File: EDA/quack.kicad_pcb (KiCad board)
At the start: 2 copper layers, 56.6 x 57.7 mm, 25 parts, among them IC1 ESP32-PICO-D4, IC2 TXB0108PWR, J1 DIN-4, J2 DB9_Male, J3 FTDI, J4 MODE, U1 AMS1117-3.3

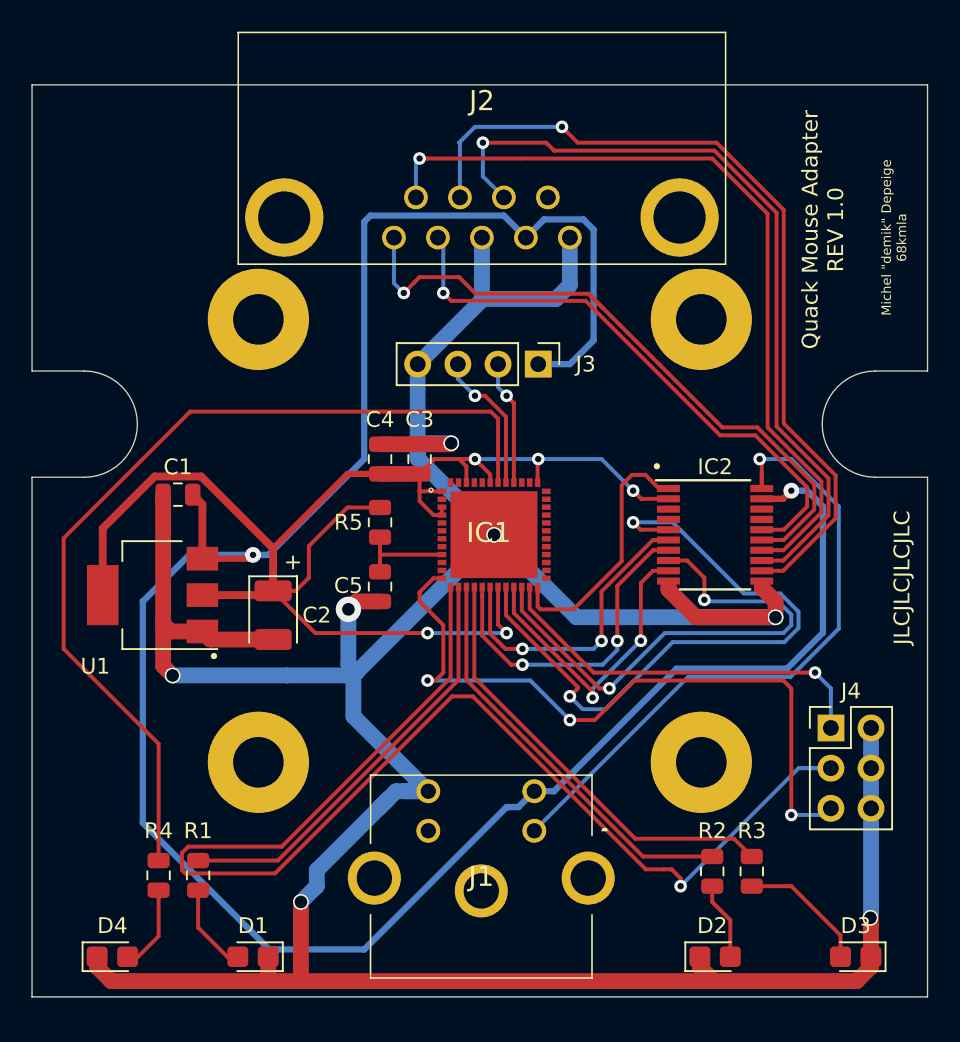
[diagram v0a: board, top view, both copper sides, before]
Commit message: added pin usage text + logos
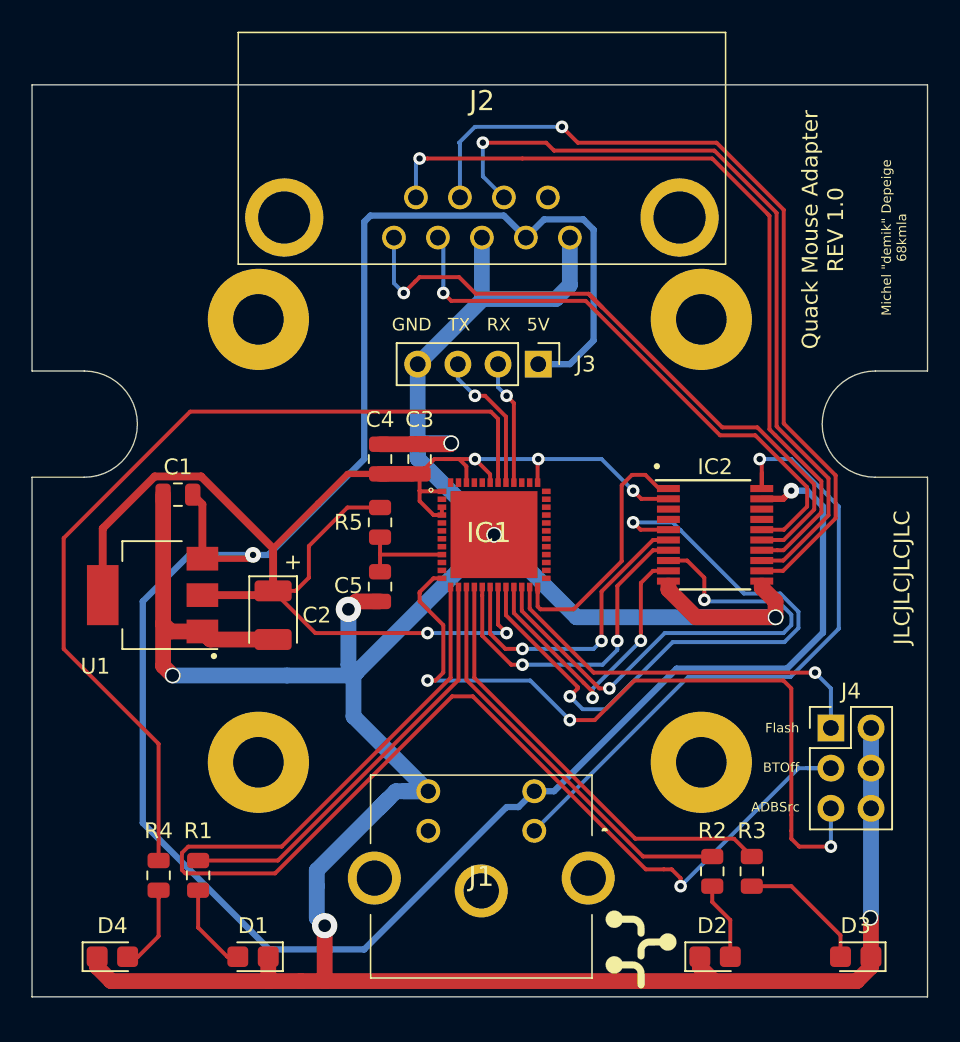
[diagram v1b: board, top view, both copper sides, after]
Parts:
- added G***: LOGO, ADB_logo_5mm:ADB_logo_5mm, F.Cu at (165.5, 124.0)
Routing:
- net ADBSRC: track 44.6 -> 49.2 mm
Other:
- board text added: "5V"
- board text added: "ADBSrc"
- board text added: "BTOff"
- board text added: "Flash"
- board text added: "GND"
- board text added: "RX"
- board text added: "TX"

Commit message: added beads to reduce EMI
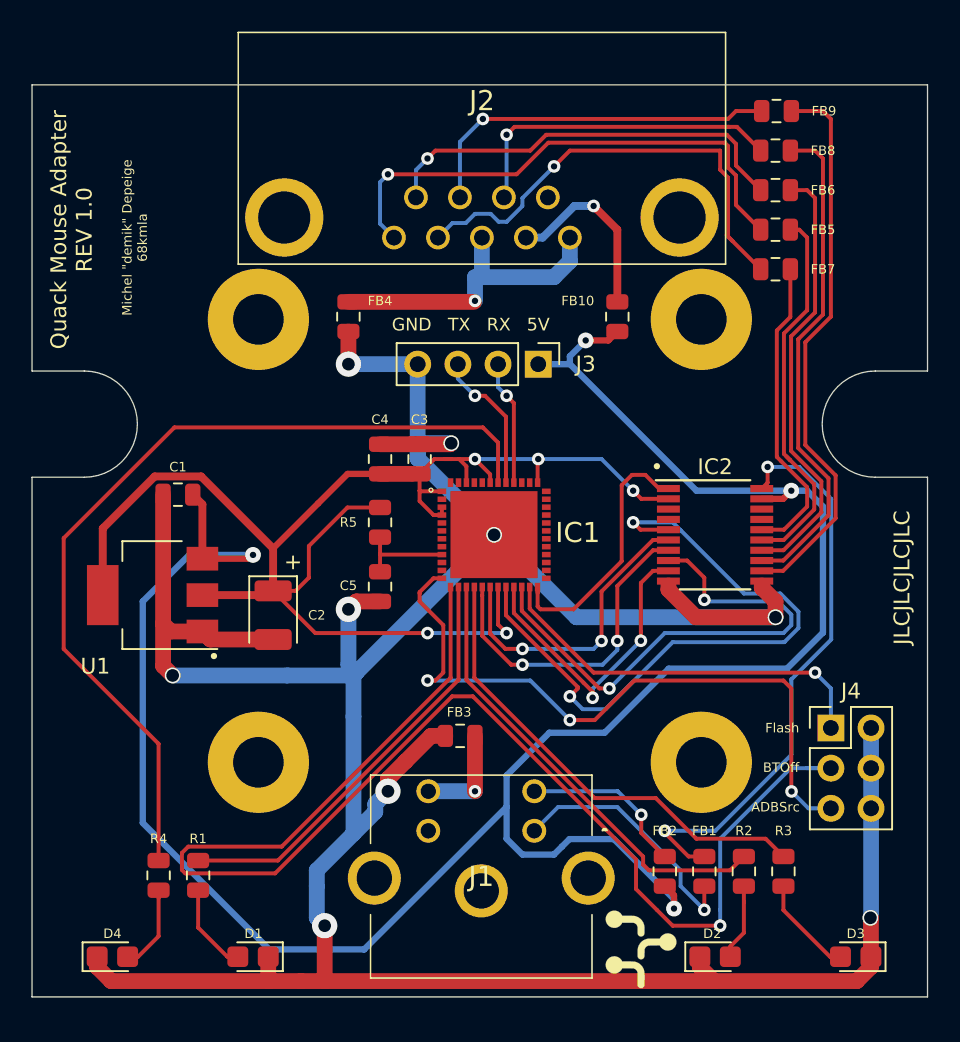
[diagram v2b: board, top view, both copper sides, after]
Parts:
- added FB1: Ferrite_Bead, Inductor_SMD:L_0805_2012Metric, F.Cu at (169.5, 119.1)
- added FB10: Ferrite_Bead_Small, Inductor_SMD:L_0805_2012Metric, F.Cu at (164.0, 84.0)
- added FB2: Ferrite_Bead, Inductor_SMD:L_0805_2012Metric, F.Cu at (167.0, 119.1)
- added FB3: Ferrite_Bead, Inductor_SMD:L_0805_2012Metric, F.Cu at (154.1, 110.5)
- added FB4: Ferrite_Bead_Small, Inductor_SMD:L_0805_2012Metric, F.Cu at (147.0, 84.0)
- added FB5: Ferrite_Bead_Small, Inductor_SMD:L_0805_2012Metric, F.Cu at (174.0, 78.5)
- added FB6: Ferrite_Bead_Small, Inductor_SMD:L_0805_2012Metric, F.Cu at (174.0, 76.0)
- added FB7: Ferrite_Bead_Small, Inductor_SMD:L_0805_2012Metric, F.Cu at (174.0, 81.0)
- added FB8: Ferrite_Bead_Small, Inductor_SMD:L_0805_2012Metric, F.Cu at (174.0, 73.5)
- added FB9: Ferrite_Bead_Small, Inductor_SMD:L_0805_2012Metric, F.Cu at (174.1, 71.0)
- moved R2 2.00 mm to (172.0, 119.1)
- moved R3 2.00 mm to (174.5, 119.1)
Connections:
- IC2 pad 20: Net-(IC2-Pad20) -> Net-(FB1-Pad2)
- J1 pad 1: Net-(IC2-Pad20) -> Net-(FB1-Pad1)
- J1 pad 3: +5V -> Net-(FB2-Pad2)
- J1 pad 4: GND -> Net-(FB3-Pad2)
- J2 pad 1: GND -> Net-(FB4-Pad2)
- J2 pad 2: +5V -> Net-(FB10-Pad1)
- J2 pad 3: GND -> Net-(FB4-Pad2)
- J2 pad 4: /quack_connectors/QX2_5V -> Net-(FB7-Pad1)
- J2 pad 5: /quack_connectors/QX1_5V -> Net-(FB5-Pad1)
- J2 pad 7: /quack_connectors/CLICK_5V -> Net-(FB8-Pad1)
- J2 pad 8: /quack_connectors/QY2_5V -> Net-(FB9-Pad1)
- J2 pad 9: /quack_connectors/QY1_5V -> Net-(FB6-Pad1)
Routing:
- net Net-(IC2-Pad20): track 41.4 -> 0.00 mm, vias 1 -> 0
- net Net-(FB1-Pad2): track 0.00 -> 36.8 mm, vias 0 -> 2
- net Net-(FB5-Pad1): track 0.00 -> 33.1 mm, vias 0 -> 1
- net Net-(FB7-Pad1): track 0.00 -> 29.9 mm, vias 0 -> 1
- net Net-(FB6-Pad1): track 0.00 -> 26.7 mm, vias 0 -> 1
- net Net-(FB9-Pad1): track 0.00 -> 23.4 mm, vias 0 -> 1
- net /quack_connectors/QY1_5V: track 51.0 -> 27.8 mm, vias 1 -> 0
- net Net-(FB8-Pad1): track 0.00 -> 21.0 mm, vias 0 -> 1
- net Net-(FB4-Pad2): track 0.00 -> 20.7 mm, vias 0 -> 1
- net /quack_connectors/CLICK_5V: track 50.3 -> 31.7 mm, vias 1 -> 0
- net /quack_connectors/QX1_5V: track 42.5 -> 24.3 mm, vias 1 -> 0
- net /quack_connectors/QY2_5V: track 53.5 -> 35.5 mm, vias 1 -> 0
- net /quack_connectors/QX2_5V: track 36.4 -> 19.6 mm, vias 1 -> 0
- net Net-(FB1-Pad1): track 0.00 -> 16.1 mm, vias 0 -> 1
- net Net-(FB10-Pad1): track 0.00 -> 11.8 mm, vias 0 -> 1
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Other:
- net class +V: via_dia 1 -> 0.8

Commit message: board revision 1.1
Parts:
- added ANT1: Antenna_Shield, RF_Antenna:Texas_SWRA117D_2.4GHz_Right, F.Cu at (134.0, 83.0)
- R1: value 33 -> 39
- R2, R3, R4: value 120 -> 150
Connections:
- IC1 pad 2: (no net) -> Net-(ANT1-Pad1)
- IC1 pad 39: (no net) -> OE
- IC2 pad 10: GND -> OE
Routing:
- net Net-(ANT1-Pad1): track 0.00 -> 24.1 mm
- net OE: track 0.00 -> 20.5 mm, vias 0 -> 2
- net GND: track 205.9 -> 196.0 mm
- net CLICK_3V: track 32.9 -> 26.1 mm
- net QX2_3V: track 42.2 -> 36.1 mm
- net +3V3: track 94.1 -> 98.1 mm, vias 5 -> 7
- net Net-(IC1-Pad42): vias 0 -> 2
- added copper zone on B.Cu, net GND
- added copper zone on F.Cu, net GND
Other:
- board text added: "Quack Mouse Adapter REV 1.1"
- board text removed: "Quack Mouse Adapter REV 1.0"

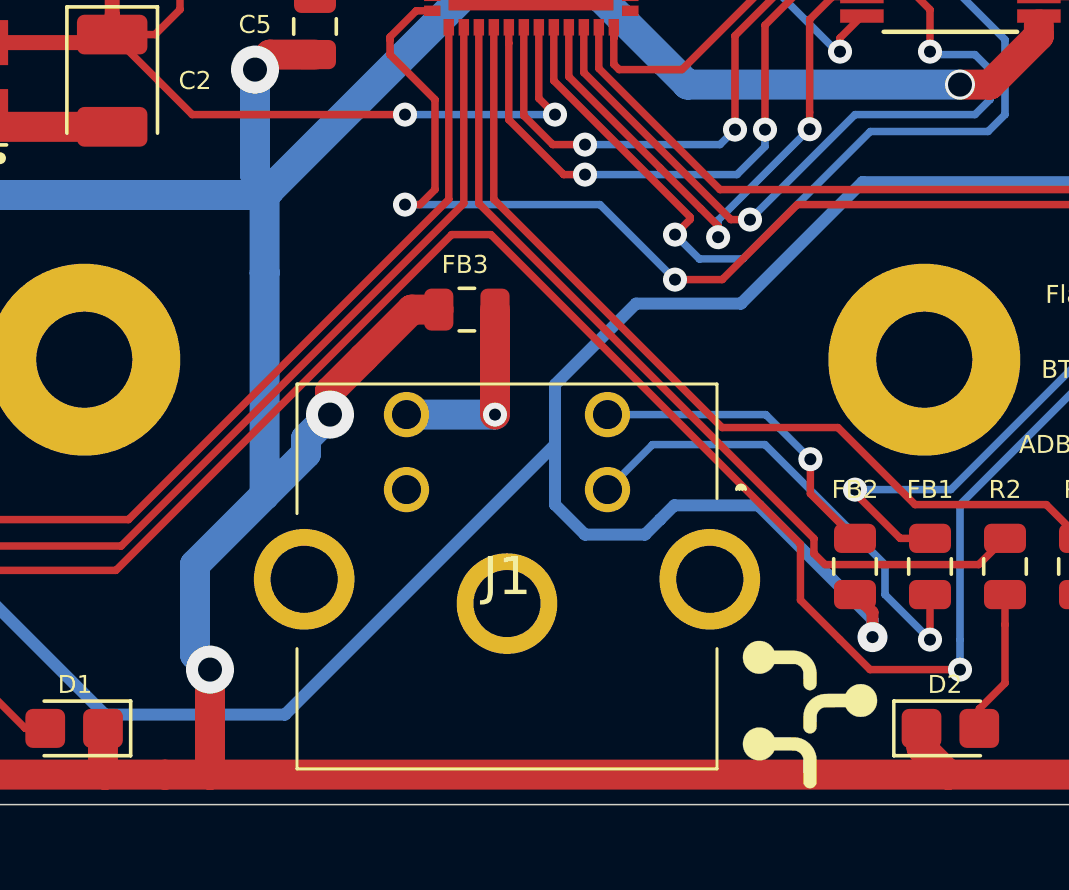
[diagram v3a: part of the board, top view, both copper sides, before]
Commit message: revision 1.2: move ADB socket 2mm out
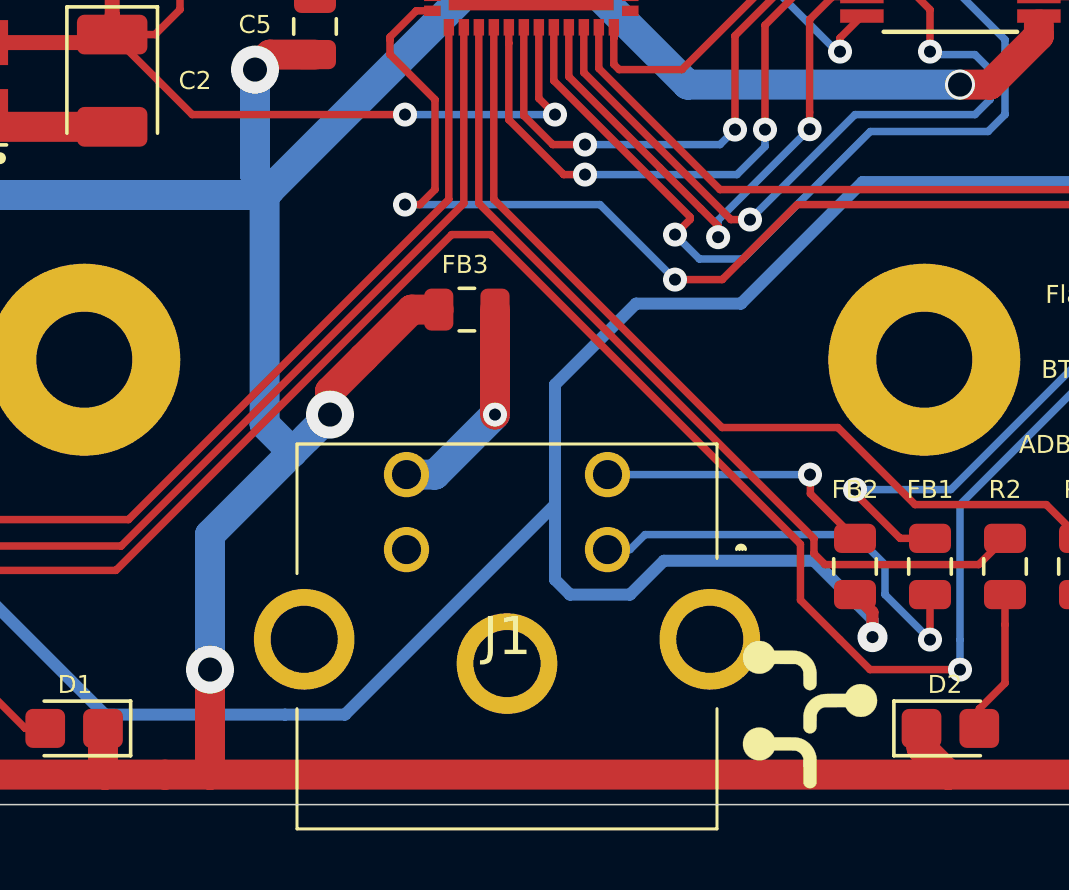
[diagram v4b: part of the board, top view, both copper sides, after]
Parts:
- moved J1 2.00 mm to (158.8, 118.5)
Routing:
- net Net-(FB1-Pad1): track 16.1 -> 14.5 mm
- net Net-(FB2-Pad2): track 10.6 -> 9.50 mm
- net Net-(FB3-Pad2): track 6.45 -> 7.28 mm
- net +5V: track 139.1 -> 139.8 mm

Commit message: Board revision 1.2
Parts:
- IC2: value TXB0108PWR -> TXS0108EPWR; footprint Package_SO:TSSOP-20_4.4x6.5mm_P0.65mm -> TXS0108EPWR:SOP65P640X120-20N
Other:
- board text added: "Quack Mouse Adapter REV 1.2"
- board text removed: "Quack Mouse Adapter REV 1.1"

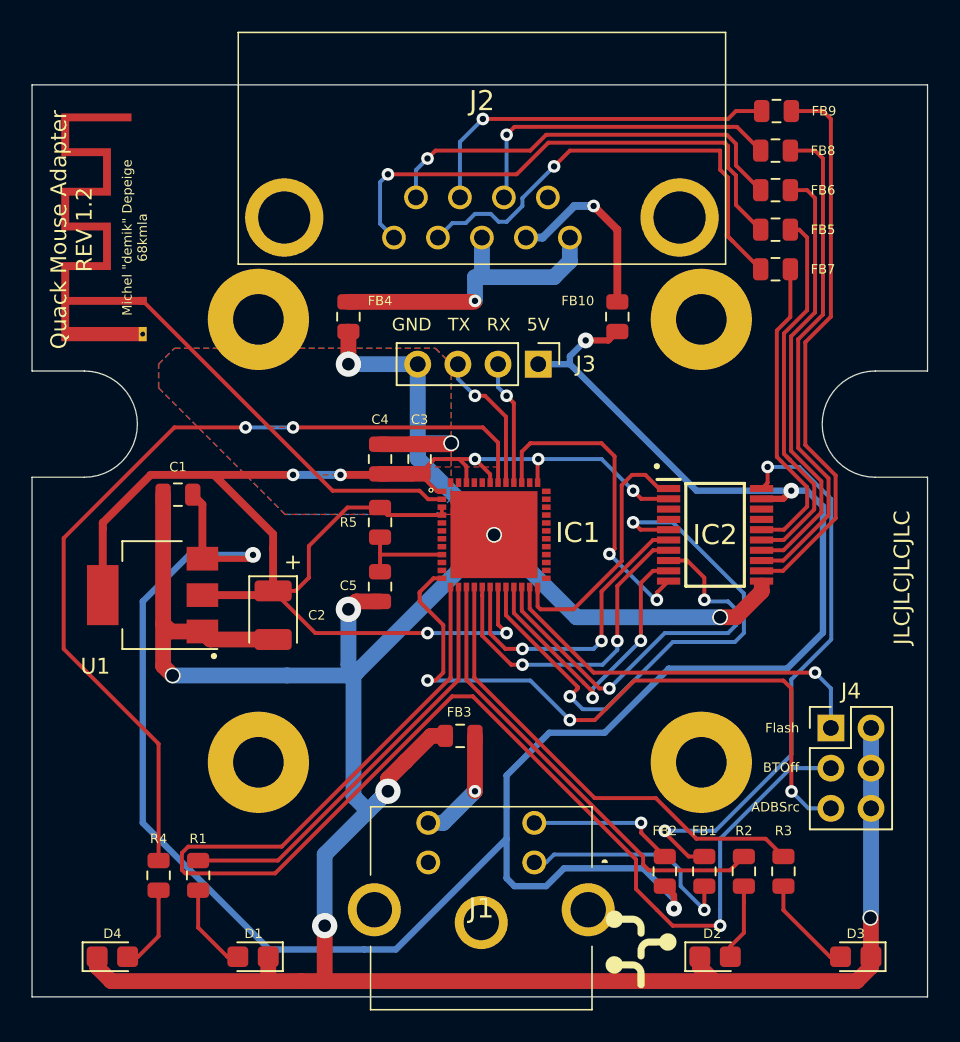
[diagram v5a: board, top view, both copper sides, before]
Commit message: replaced RXS0108EPWR by 74LVC2T45 + 74LVC4245
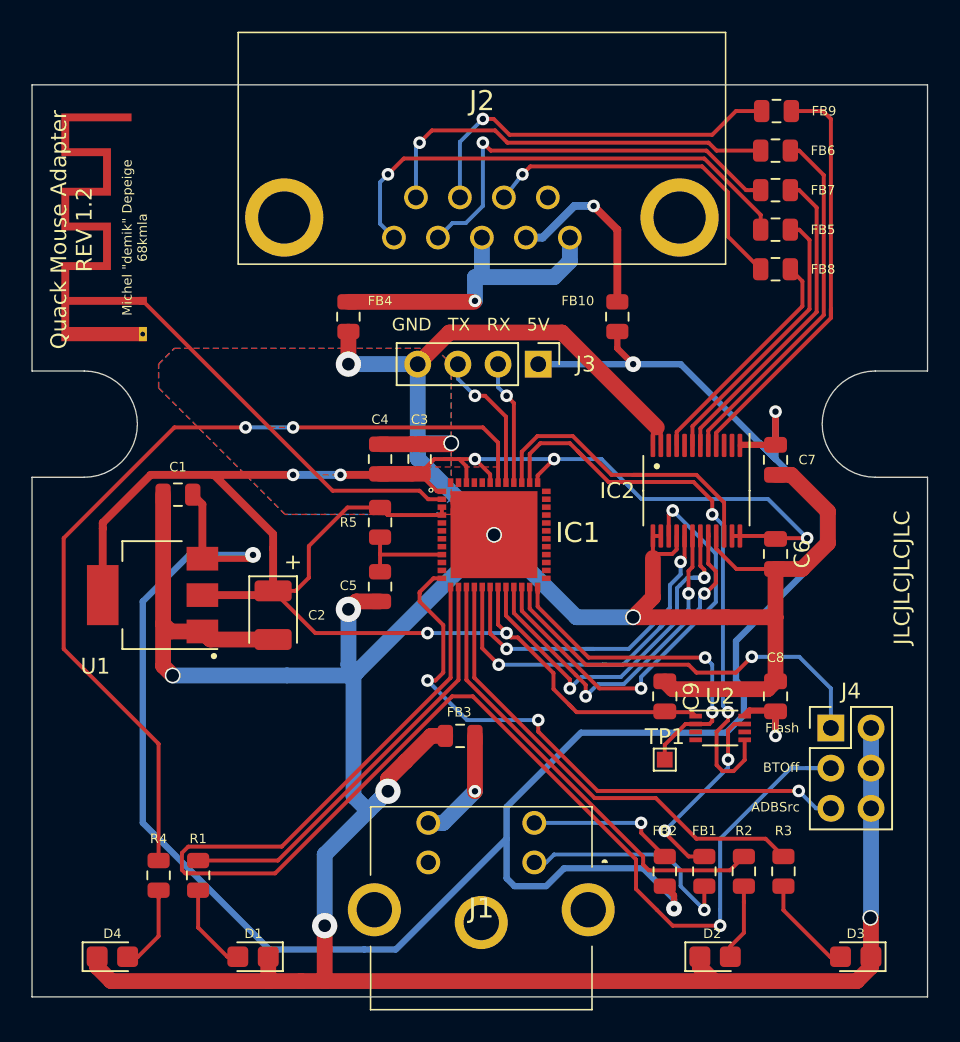
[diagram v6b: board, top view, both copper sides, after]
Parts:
- removed G***: LOGO, ADB_logo_5mm:ADB_logo_5mm
- removed REF** (x4): MountingHole_3.2mm_M3_Pad, MountingHole:MountingHole_3.2mm_M3_Pad
- added C6: 100nF, Capacitor_SMD:C_0805_2012Metric, F.Cu at (174.0, 99.0)
- added C7: 100nF, Capacitor_SMD:C_0805_2012Metric, F.Cu at (174.0, 93.0)
- added C8: 100nF, Capacitor_SMD:C_0805_2012Metric, F.Cu at (174.0, 108.0)
- added C9: 100nF, Capacitor_SMD:C_0805_2012Metric, F.Cu at (167.0, 108.0)
- added TP1: TestPoint ADB ESP32, TestPoint:TestPoint_Pad_1.0x1.0mm, F.Cu at (167.0, 112.0)
- added U2: 74LVC2T45DC, Package_SO:VSSOP-8_2.3x2mm_P0.5mm, F.Cu at (170.5, 110.0)
- C5: value 0.1uF -> 100nF
- IC2: value TXS0108EPWR -> SN74LVC4245APWR; footprint TXS0108EPWR:SOP65P640X120-20N -> Package_SO:TSSOP-24_4.4x6.5mm_P0.5mm
- R1: value 39 -> 68
- moved FB8 7.50 mm to (174.0, 81.0)
- moved FB7 5.00 mm to (174.0, 76.0)
- moved IC2 3.03 mm to (169.0, 95.0), turned to 270 degrees
- moved FB6 2.50 mm to (174.0, 73.5)
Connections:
- IC1 pad 38: (no net) -> DIR
- IC1 pad 39: OE -> ~OE
- IC2 pad 1: ADB -> +5V
- IC2 pad 10: OE -> (no net)
- IC2 pad 12: /quack_connectors/QY2_5V -> GND
- IC2 pad 13: /quack_connectors/CLICK_5V -> GND
- IC2 pad 14: /quack_connectors/QY1_5V -> GND
- IC2 pad 15: /quack_connectors/QX1_5V -> CLICK_3V
- IC2 pad 16: /quack_connectors/QX2_5V -> GND
- IC2 pad 17: (no net) -> QX1_3V
- IC2 pad 18: (no net) -> QX2_3V
- IC2 pad 19: +5V -> QY1_3V
- IC2 pad 2: +3V3 -> (no net)
- IC2 pad 20: Net-(FB1-Pad2) -> QY2_3V
- IC2 pad 4: (no net) -> /quack_connectors/QY2_5V
- IC2 pad 5: QX2_3V -> /quack_connectors/QY1_5V
- IC2 pad 6: QX1_3V -> /quack_connectors/QX2_5V
- IC2 pad 7: QY1_3V -> /quack_connectors/QX1_5V
- IC2 pad 8: CLICK_3V -> (no net)
- IC2 pad 9: QY2_3V -> /quack_connectors/CLICK_5V
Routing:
- net GND: track 195.7 -> 255.1 mm
- net DIR: track 0.00 -> 36.8 mm, vias 0 -> 2
- net +3V3: track 98.1 -> 128.1 mm
- net Net-(FB1-Pad2): track 36.8 -> 12.5 mm
- net OE: track 20.5 -> 0.00 mm, vias 2 -> 0
- net ~OE: track 0.00 -> 19.5 mm
- net /quack_connectors/CLICK_5V: track 31.7 -> 14.7 mm
- net QX2_3V: track 36.1 -> 22.4 mm
- net +5V: track 139.8 -> 149.3 mm, vias 4 -> 5
- net /quack_connectors/QY2_5V: track 35.5 -> 26.8 mm
- net /quack_connectors/QX1_5V: track 24.3 -> 17.5 mm
- net ADB: track 16.6 -> 22.3 mm, vias 0 -> 2
- net ADBSRC: track 44.0 -> 38.6 mm
- net /quack_connectors/QY1_5V: track 27.8 -> 22.9 mm
- net QY1_3V: track 21.0 -> 25.4 mm
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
